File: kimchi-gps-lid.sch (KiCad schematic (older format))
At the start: 8 parts, among them J1 DF40HC(3.5)-60DS, J2 DF40HC(3.5)-60DS, U1 24C32

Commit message: Creating Schematic for the GPS LID
Addition of schematic, datasheets,footprints and 3D Files.

Signed of by: Thore Krug opensource[at]thorekrug.de
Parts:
- added BT1: BAT-HLD-012-SMT, BAT_BAT-HLD-012-SMT, symbol BAT-HLD-012-SMT:BAT-HLD-012-SMT
- added C1, C2, C4, C5, C6: 100n, symbol Device:C
- added C3: 10uF, symbol Device:C
- added D1: LED, symbol Device:LED
- added Q1, Q2: DTC143ZEBTL, SOTFL50P160X85-3N, symbol DTC143ZEBTL:DTC143ZEBTL
- added R1: 10K, symbol Device:R
- added R2: R, symbol Device:R
- added U2: L80RE-M37, XCVR_L80RE-M37, symbol L80RE-M37:L80RE-M37
- added U3: TXS0104ED, SOIC127P600X175-14N, symbol TXS0104ED:TXS0104ED
- H1, H2, H3, H4: symbol Mechanical:MountingHole_Pad -> kimchi-gps-lid-rescue:MountingHole_Pad-Mechanical
- J1, J2: symbol Connector_Generic:Conn_02x30_Counter_Clockwise -> kimchi-gps-lid-rescue:Conn_02x30_Counter_Clockwise-Connector_Generic
- LOGO1: symbol Graphic:Logo_Open_Hardware_Small -> kimchi-gps-lid-rescue:Logo_Open_Hardware_Small-Graphic
- U1: symbol Memory_EEPROM:24LC16 -> kimchi-gps-lid-rescue:24LC16-Memory_EEPROM
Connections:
- net GND: now also BT1.N, C1.2, C2.2, C3.2, C4.2, C5.2, C6.2, Q1.2, Q2.2, R1.2, U2.12 (GND), U2.3 (GND), U3.7 (GND)
- net GPIO1[14]: now also R1.1, U3.8 (OE)
- net GPIO1[15]: now also U3.4 (A3)
- net UART3_RX: now also U3.3 (A2)
- net UART3_TX: now also U3.2 (A1)
- net VDD_1V8: now also C2.1, U3.1 (VCCA)
- net VDD_3V3: now also C1.1, C3.1, C4.1, R2.1, U2.4 (VCC), U3.14 (VCCB)
- new net: D1.1 (K), Q2.3
- new net: D1.2 (A), R2.2
- new net 1PPS: Q2.1, U2.6 (1PPS)
- new net RESET: Q1.3, U2.10 (RESET)
- new net RESET-GPIO: Q1.1, U3.11 (B3)
- new net RXD1: U2.1 (RXD1), U3.13 (B1)
- new net TXD1: U2.2 (TXD1), U3.12 (B2)
- new net V_BCKP: BT1.P1, BT1.P2, C5.1, C6.1, U2.5 (V_BCKP)
- no-connect marks 0 -> 3
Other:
- note added: "Backup Battery"
- note added: "L80-R or LC86L GPS/GNSS Module\n"
- note added: "Level Shifter IC"
- note added: "Place 100n near the GPS module\n"
- note added: "Place 100nF near the GPS Module"
- note added: "Place Capacitors close to the Level Shifter \n"
- note added: "Reset Circuitry and LED Activity Indication"
- note added: "What LED Color ? \nDiscuss then size R accordingly"

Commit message: Fix Capacitor Value
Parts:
- C5: value 100n -> 4,7uF
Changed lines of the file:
@@
 P 8200 8150
 F 0 "C5" H 8315 8196 50  0000 L CNN
-F 1 "100n" H 8315 8105 50  0000 L CNN
+F 1 "4,7uF" H 8315 8105 50  0000 L CNN
 F 2 "" H 8238 8000 50  0001 C CNN
 F 3 "~" H 8200 8150 50  0001 C CNN

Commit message: Completed routing, minor fixes remaining
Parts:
- BT1: footprint BAT_BAT-HLD-012-SMT -> gps:BAT_BAT-HLD-012-SMT
- C1, C2, C3, C4, C5, C6: footprint (none) -> Capacitor_SMD:C_0603_1608Metric
- D1: footprint (none) -> LED_SMD:LED_0603_1608Metric
- Q1, Q2: footprint SOTFL50P160X85-3N -> gps:SOTFL50P160X85-3N
- R1, R2: footprint (none) -> Resistor_SMD:R_0603_1608Metric
- U2: footprint XCVR_L80RE-M37 -> gps:XCVR_L80RE-M37
- U3: footprint SOIC127P600X175-14N -> gps:SOIC127P600X175-14N
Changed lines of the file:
@@
 F 0 "U2" H 5000 6617 50  0000 C CNN
 F 1 "L80RE-M37" H 5000 6526 50  0000 C CNN
-F 2 "XCVR_L80RE-M37" H 5000 5850 50  0001 L BNN
+F 2 "gps:XCVR_L80RE-M37" H 5000 5850 50  0001 L BNN
 F 3 "" H 5000 5850 50  0001 L BNN
 F 4 "Quectel" H 5000 5850 50  0001 L BNN "MF"
@@
 F 0 "U3" H 9150 6470 50  0000 C CNN
 F 1 "TXS0104ED" H 9150 6379 50  0000 C CNN
-F 2 "SOIC127P600X175-14N" H 9150 5700 50  0001 L BNN
+F 2 "gps:SOIC127P600X175-14N" H 9150 5700 50  0001 L BNN
 F 3 "" H 9150 5700 50  0001 L BNN
 	1    9150 5700
@@
 F 0 "Q2" H 5494 8846 50  0000 L CNN
 F 1 "DTC143ZEBTL" H 5494 8755 50  0000 L CNN
-F 2 "SOTFL50P160X85-3N" H 5350 8800 50  0001 L BNN
+F 2 "gps:SOTFL50P160X85-3N" H 5350 8800 50  0001 L BNN
 F 3 "" H 5350 8800 50  0001 L BNN
 F 4 "ROHM" H 5350 8800 50  0001 L BNN "MANUFACTURER"
@@
 F 0 "Q1" H 3694 8796 50  0000 L CNN
 F 1 "DTC143ZEBTL" H 3694 8705 50  0000 L CNN
-F 2 "SOTFL50P160X85-3N" H 3550 8750 50  0001 L BNN
+F 2 "gps:SOTFL50P160X85-3N" H 3550 8750 50  0001 L BNN
 F 3 "" H 3550 8750 50  0001 L BNN
 F 4 "ROHM" H 3550 8750 50  0001 L BNN "MANUFACTURER"
@@
 F 0 "D1" V 5289 7982 50  0000 R CNN
 F 1 "LED" V 5198 7982 50  0000 R CNN
-F 2 "" H 5250 8100 50  0001 C CNN
+F 2 "LED_SMD:LED_0603_1608Metric" H 5250 8100 50  0001 C CNN
 F 3 "~" H 5250 8100 50  0001 C CNN
 	1    5250 8100
@@
 F 0 "R2" H 5320 7696 50  0000 L CNN
 F 1 "R" H 5320 7605 50  0000 L CNN
-F 2 "" V 5180 7650 50  0001 C CNN
+F 2 "Resistor_SMD:R_0603_1608Metric" V 5180 7650 50  0001 C CNN
 F 3 "~" H 5250 7650 50  0001 C CNN
 	1    5250 7650
@@
 F 0 "R1" H 10120 6246 50  0000 L CNN
 F 1 "10K" H 10120 6155 50  0000 L CNN
-F 2 "" V 9980 6200 50  0001 C CNN
+F 2 "Resistor_SMD:R_0603_1608Metric" V 9980 6200 50  0001 C CNN
 F 3 "~" H 10050 6200 50  0001 C CNN
 	1    10050 6200
@@
 F 0 "C4" H 2715 5846 50  0000 L CNN
 F 1 "100n" H 2715 5755 50  0000 L CNN
-F 2 "" H 2638 5650 50  0001 C CNN
+F 2 "Capacitor_SMD:C_0603_1608Metric" H 2638 5650 50  0001 C CNN
 F 3 "~" H 2600 5800 50  0001 C CNN
 	1    2600 5800
@@
 F 0 "C3" H 3365 5846 50  0000 L CNN
 F 1 "10uF" H 3365 5755 50  0000 L CNN
-F 2 "" H 3288 5650 50  0001 C CNN
+F 2 "Capacitor_SMD:C_0603_1608Metric" H 3288 5650 50  0001 C CNN
 F 3 "~" H 3250 5800 50  0001 C CNN
 	1    3250 5800
@@
 F 0 "C2" H 11365 5696 50  0000 L CNN
 F 1 "100n" H 11365 5605 50  0000 L CNN
-F 2 "" H 11288 5500 50  0001 C CNN
+F 2 "Capacitor_SMD:C_0603_1608Metric" H 11288 5500 50  0001 C CNN
 F 3 "~" H 11250 5650 50  0001 C CNN
 	1    11250 5650
@@
 F 0 "C1" H 11915 5696 50  0000 L CNN
 F 1 "100n" H 11915 5605 50  0000 L CNN
-F 2 "" H 11838 5500 50  0001 C CNN
+F 2 "Capacitor_SMD:C_0603_1608Metric" H 11838 5500 50  0001 C CNN
 F 3 "~" H 11800 5650 50  0001 C CNN
 	1    11800 5650
@@
 F 0 "BT1" V 9104 8280 50  0000 L CNN
 F 1 "BAT-HLD-012-SMT" V 9195 8280 50  0000 L CNN
-F 2 "BAT_BAT-HLD-012-SMT" H 9150 8150 50  0001 L BNN
+F 2 "gps:BAT_BAT-HLD-012-SMT" H 9150 8150 50  0001 L BNN
 F 3 "" H 9150 8150 50  0001 L BNN
 F 4 "A" H 9150 8150 50  0001 L BNN "PARTREV"
@@
 F 0 "C5" H 8315 8196 50  0000 L CNN
 F 1 "4,7uF" H 8315 8105 50  0000 L CNN
-F 2 "" H 8238 8000 50  0001 C CNN
+F 2 "Capacitor_SMD:C_0603_1608Metric" H 8238 8000 50  0001 C CNN
 F 3 "~" H 8200 8150 50  0001 C CNN
 	1    8200 8150
@@
 F 0 "C6" H 8815 8196 50  0000 L CNN
 F 1 "100n" H 8815 8105 50  0000 L CNN
-F 2 "" H 8738 8000 50  0001 C CNN
+F 2 "Capacitor_SMD:C_0603_1608Metric" H 8738 8000 50  0001 C CNN
 F 3 "~" H 8700 8150 50  0001 C CNN
 	1    8700 8150

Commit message: Update layout and routing
Signed-off-by: Michael Welling <mwelling@ieee.org>
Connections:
- net GPIO1[15]: now also U3.2 (A1); no longer U3.4 (A3)
- net RESET-GPIO: now also U3.13 (B1); no longer U3.11 (B3)
- net RXD1: now also U3.12 (B2); no longer U3.13 (B1)
- net TXD1: now also U3.11 (B3); no longer U3.12 (B2)
- net UART3_RX: now also U3.4 (A3); no longer U3.3 (A2)
- net UART3_TX: now also U3.3 (A2); no longer U3.2 (A1)
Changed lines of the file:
@@
 	-1   0    0    -1
 $EndComp
-Wire Wire Line
-	8450 5500 7150 5500
-Wire Wire Line
-	7250 5600 8450 5600
-Text GLabel 10100 5600 2    50   Input ~ 0
+Text GLabel 10100 5700 2    50   Input ~ 0
 UART3_RX
-Text Label 7650 5500 0    50   ~ 0
+Text Label 8250 5600 0    50   ~ 0
 RXD1
-Text Label 7650 5600 0    50   ~ 0
+Text Label 8250 5700 0    50   ~ 0
 TXD1
 $Comp
@@
 	1    0    0    -1
 $EndComp
-Text GLabel 8200 5700 0    50   Output ~ 0
+Text GLabel 8200 5500 0    50   Output ~ 0
 RESET-GPIO
 Wire Wire Line
-	8450 5700 8200 5700
+	8450 5500 8200 5500
 Text GLabel 5900 5650 2    50   Input ~ 0
 RESET
@@
 Text Notes 8950 4750 0    50   ~ 10
 Level Shifter IC
+Text GLabel 10100 5600 2    50   Input ~ 0
+UART3_TX
+Wire Wire Line
+	9850 5500 10100 5500
+Wire Wire Line
+	5700 6150 7250 6150
+Wire Wire Line
+	7150 6050 5700 6050
+Wire Wire Line
+	9850 5600 10100 5600
 Text GLabel 10100 5500 2    50   Input ~ 0
-UART3_TX
-Wire Wire Line
-	9850 5500 10100 5500
-Wire Wire Line
-	5700 6150 7250 6150
-Wire Wire Line
-	7150 6050 5700 6050
-Wire Wire Line
-	7250 6150 7250 5600
-Wire Wire Line
-	7150 5500 7150 6050
-Wire Wire Line
-	9850 5600 10100 5600
-Text GLabel 10100 5700 2    50   Input ~ 0
 GPIO1[15]
 Wire Wire Line
@@
 Text Notes 8000 8950 0    50   ~ 0
 Place 100n near the GPS module\n
+Wire Wire Line
+	7150 5600 7150 6050
+Wire Wire Line
+	7150 5600 8450 5600
+Wire Wire Line
+	7250 6150 7250 5700
+Wire Wire Line
+	7250 5700 8450 5700
 $EndSCHEMATC

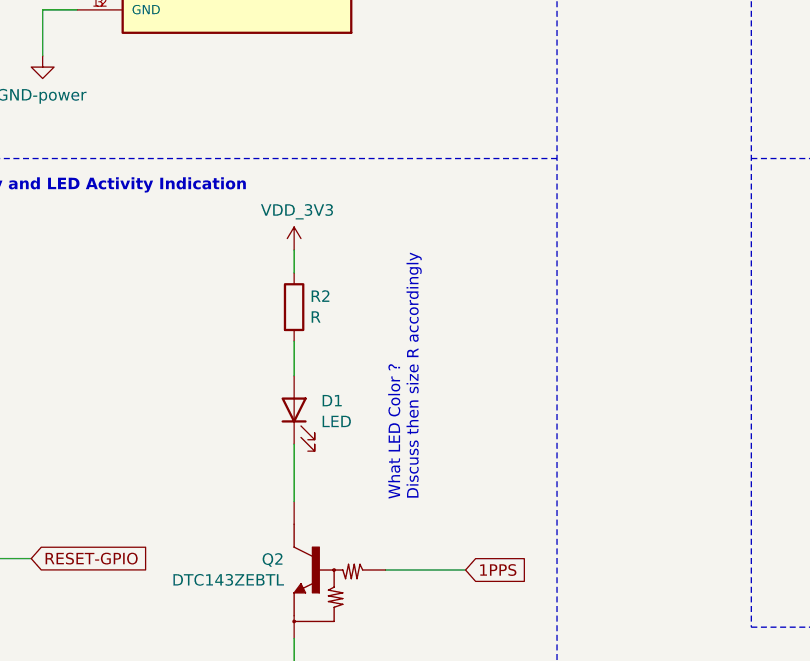
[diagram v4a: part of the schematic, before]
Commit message: Changed value of LED resistor according to requirements of green LED
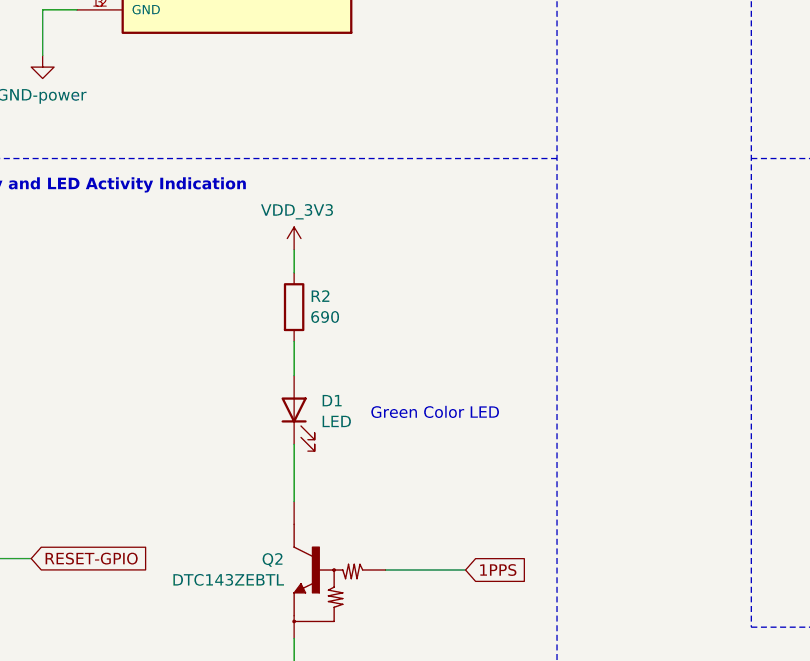
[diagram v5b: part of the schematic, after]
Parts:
- R2: value R -> 690
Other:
- note added: "Green Color LED"
- note removed: "What LED Color ? \nDiscuss then size R accordingly"
